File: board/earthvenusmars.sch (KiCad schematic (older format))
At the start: 24 parts, among them J4 Conn_01x04, SW1 SW_SPST, SW2 SW_SPST, SW3 SW_SPST, U1 ATSAMD21G18A-AU, U2 MIC5504-3.3YM5, Y1 32768Hz

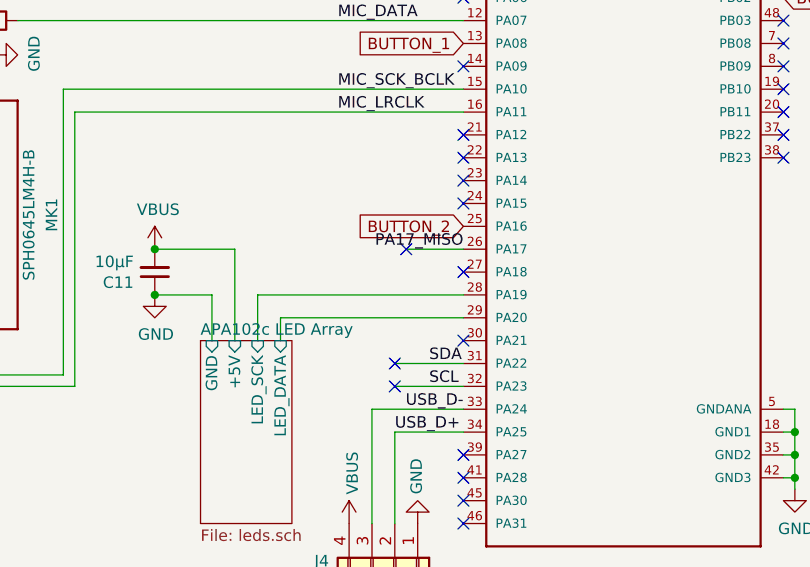
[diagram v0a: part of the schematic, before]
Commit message: move button 2 to pin 30 to avoid a via
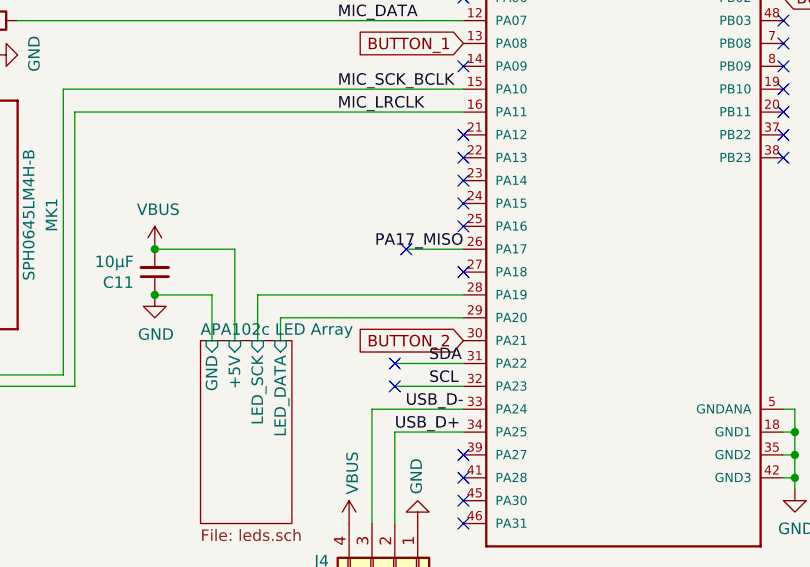
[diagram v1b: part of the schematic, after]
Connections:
- net BUTTON_2: now also U1.30 (PA21); no longer U1.25 (PA16)
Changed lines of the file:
@@
 NoConn ~ 5350 2950
 NoConn ~ 3950 3450
-NoConn ~ 3950 3750
+NoConn ~ 3950 3250
 NoConn ~ 3950 4250
 NoConn ~ 3950 4350
@@
 Text GLabel 3950 2450 0    50   Input ~ 0
 BUTTON_1
-Text GLabel 3950 3250 0    50   Input ~ 0
+Text GLabel 3950 3750 0    50   Input ~ 0
 BUTTON_2
 Text GLabel 5350 2250 2    50   Input ~ 0

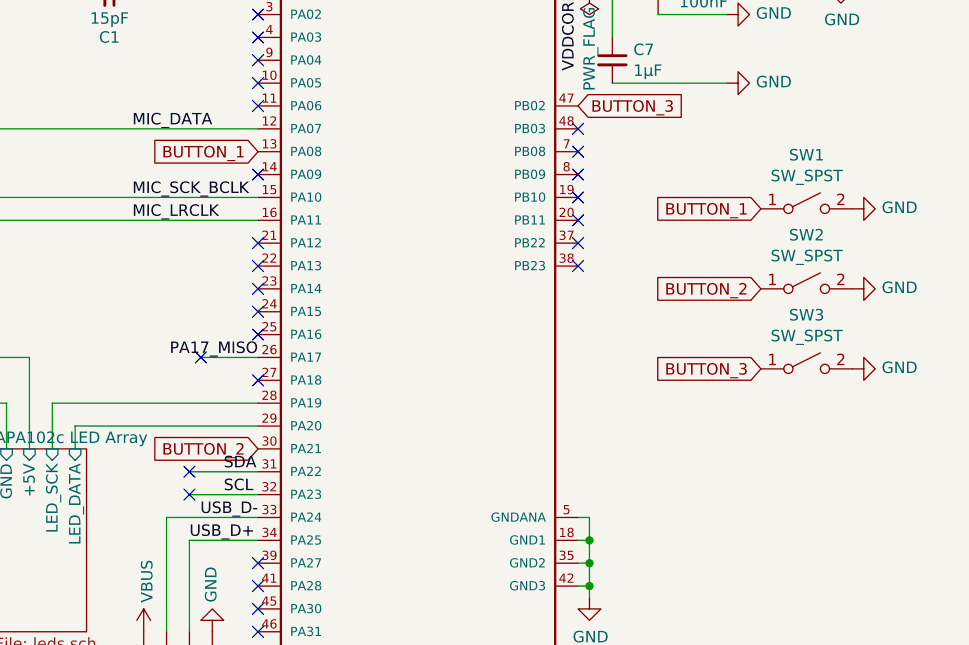
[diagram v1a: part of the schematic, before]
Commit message: proof of concept for entering low-power state when the brightness dial is all the way down, using the adc, then waking the system back up when the brightness dial is turned up again
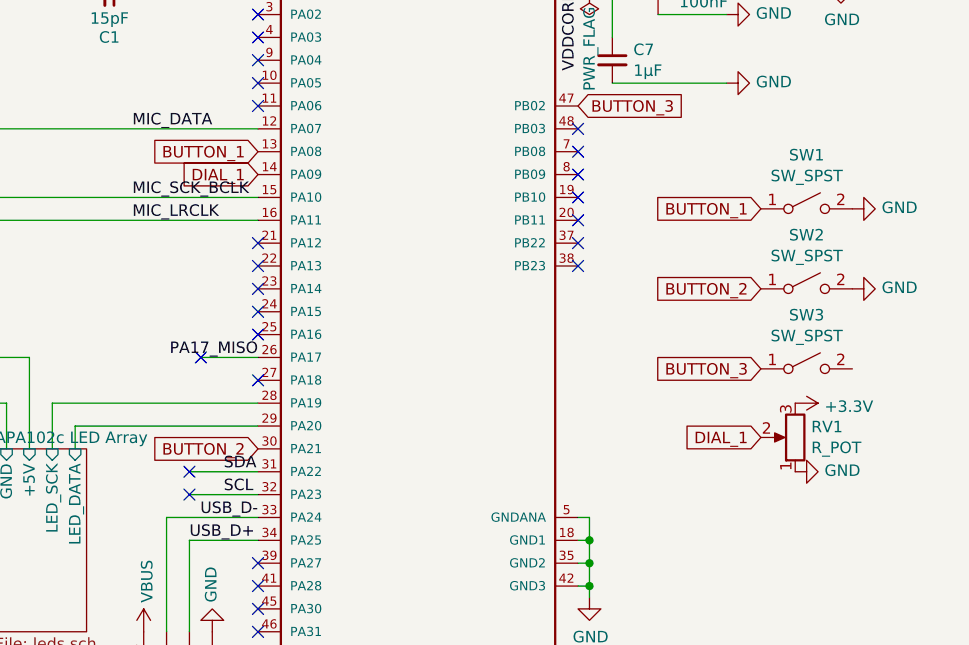
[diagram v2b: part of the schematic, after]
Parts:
- added RV1: R_POT, Pot_dial_3352T-1-103LF:Pot_dial_3352T-1-103LF, symbol Device:R_POT
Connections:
- net +3V3: now also RV1.3
- net GND: now also RV1.1; no longer SW3.2 (B)
- net DIAL_1: now reaches U1.14 (PA09)
- net DIAL_1: now also RV1.2
- no-connect marks 26 -> 25
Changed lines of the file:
@@
 NoConn ~ 3950 2950
 NoConn ~ 3950 2850
-NoConn ~ 3950 2550
 NoConn ~ 3950 2250
 NoConn ~ 3950 2150
@@
 $EndComp
 $Comp
-L power:GND #PWR?
+L power:GND #PWR0133
 U 1 1 5F9110A0
 P 6550 2700
-F 0 "#PWR?" H 6550 2450 50  0001 C CNN
+F 0 "#PWR0133" H 6550 2450 50  0001 C CNN
 F 1 "GND" V 6555 2572 50  0000 R CNN
 F 2 "" H 6550 2700 50  0001 C CNN
@@
 $EndComp
 $Comp
-L power:GND #PWR?
+L power:GND #PWR0134
 U 1 1 5F911146
 P 6550 3050
-F 0 "#PWR?" H 6550 2800 50  0001 C CNN
+F 0 "#PWR0134" H 6550 2800 50  0001 C CNN
 F 1 "GND" V 6555 2922 50  0000 R CNN
 F 2 "" H 6550 3050 50  0001 C CNN
@@
 $EndComp
 $Comp
-L power:GND #PWR?
+L power:GND #PWR0135
 U 1 1 5F9113D1
-P 6550 3400
-F 0 "#PWR?" H 6550 3150 50  0001 C CNN
-F 1 "GND" V 6555 3272 50  0000 R CNN
-F 2 "" H 6550 3400 50  0001 C CNN
-F 3 "" H 6550 3400 50  0001 C CNN
-	1    6550 3400
+P 6300 3850
+F 0 "#PWR0135" H 6300 3600 50  0001 C CNN
+F 1 "GND" V 6305 3722 50  0000 R CNN
+F 2 "" H 6300 3850 50  0001 C CNN
+F 3 "" H 6300 3850 50  0001 C CNN
+	1    6300 3850
 	0    -1   -1   0
 $EndComp
@@
 Text GLabel 6150 2700 0    50   Input ~ 0
 BUTTON_1
+$Comp
+L Device:R_POT RV1
+U 1 1 5FA0CDD3
+P 6300 3700
+F 0 "RV1" H 6230 3654 50  0000 R CNN
+F 1 "R_POT" H 6230 3745 50  0000 R CNN
+F 2 "Pot_dial_3352T-1-103LF:Pot_dial_3352T-1-103LF" H 6300 3700 50  0001 C CNN
+F 3 "~" H 6300 3700 50  0001 C CNN
+	1    6300 3700
+	-1   0    0    1
+$EndComp
+Text GLabel 3950 2550 0    50   Input ~ 0
+DIAL_1
+Text GLabel 6150 3700 0    50   Input ~ 0
+DIAL_1
+$Comp
+L power:+3.3V #PWR0136
+U 1 1 5FBE3505
+P 6300 3550
+F 0 "#PWR0136" H 6300 3400 50  0001 C CNN
+F 1 "+3.3V" V 6315 3678 50  0000 L CNN
+F 2 "" H 6300 3550 50  0001 C CNN
+F 3 "" H 6300 3550 50  0001 C CNN
+	1    6300 3550
+	0    1    1    0
+$EndComp
 $EndSCHEMATC

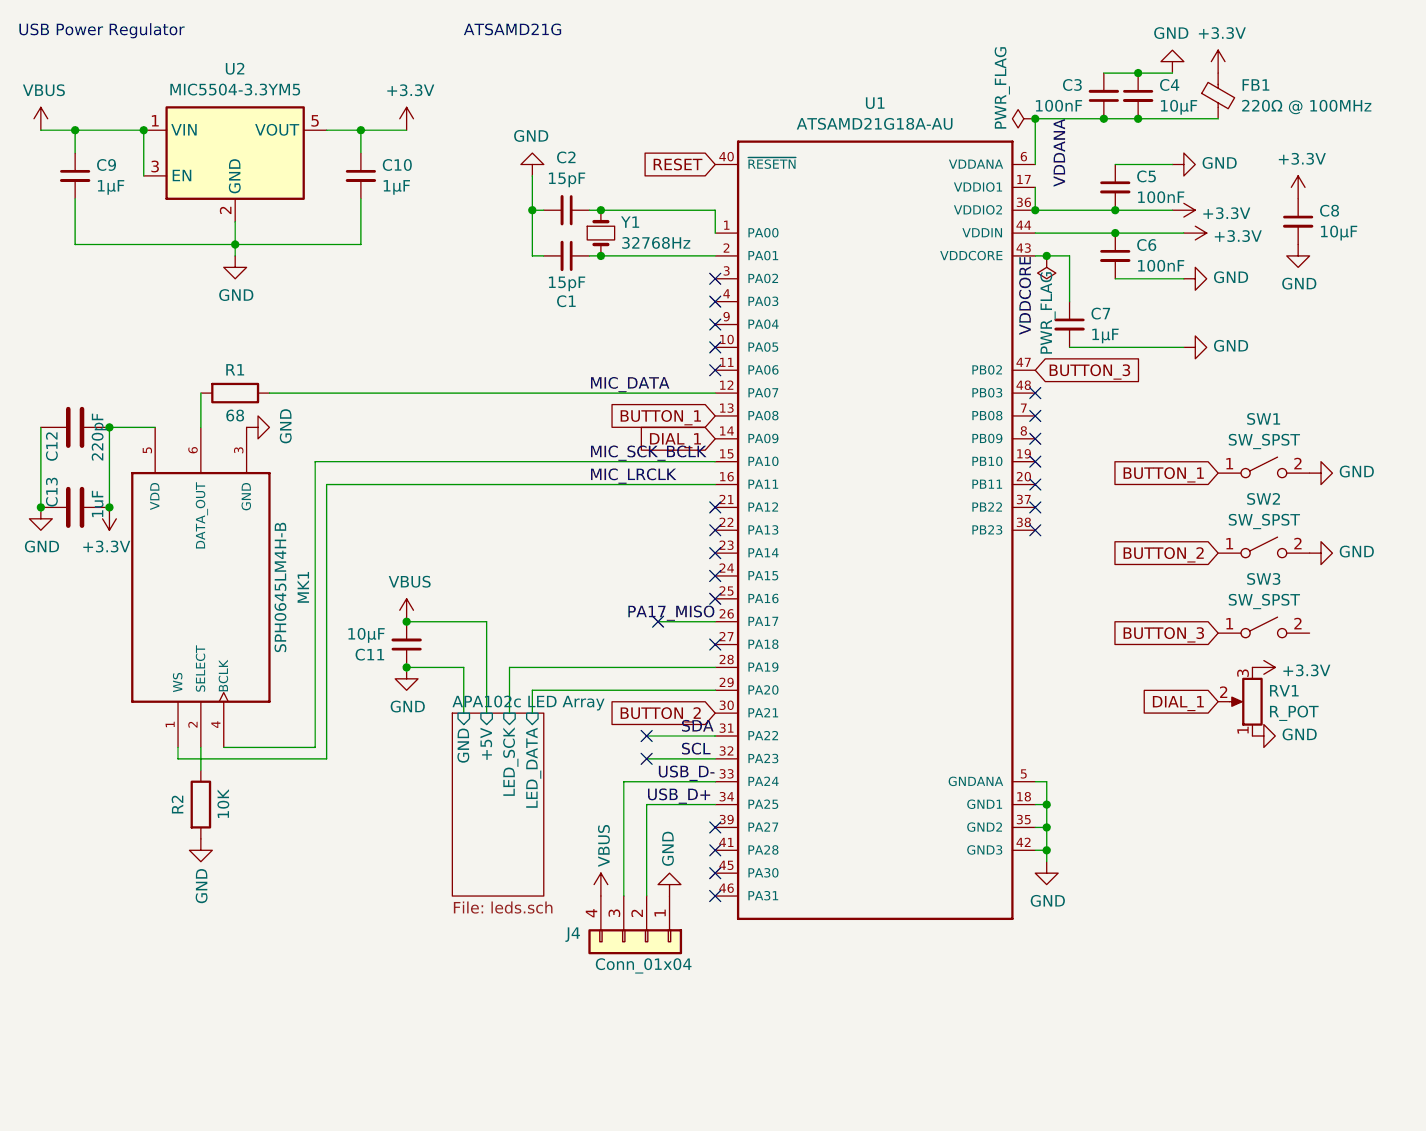
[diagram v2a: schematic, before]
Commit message: add pads on back for bootloader programming/reset and for driving the leds externally
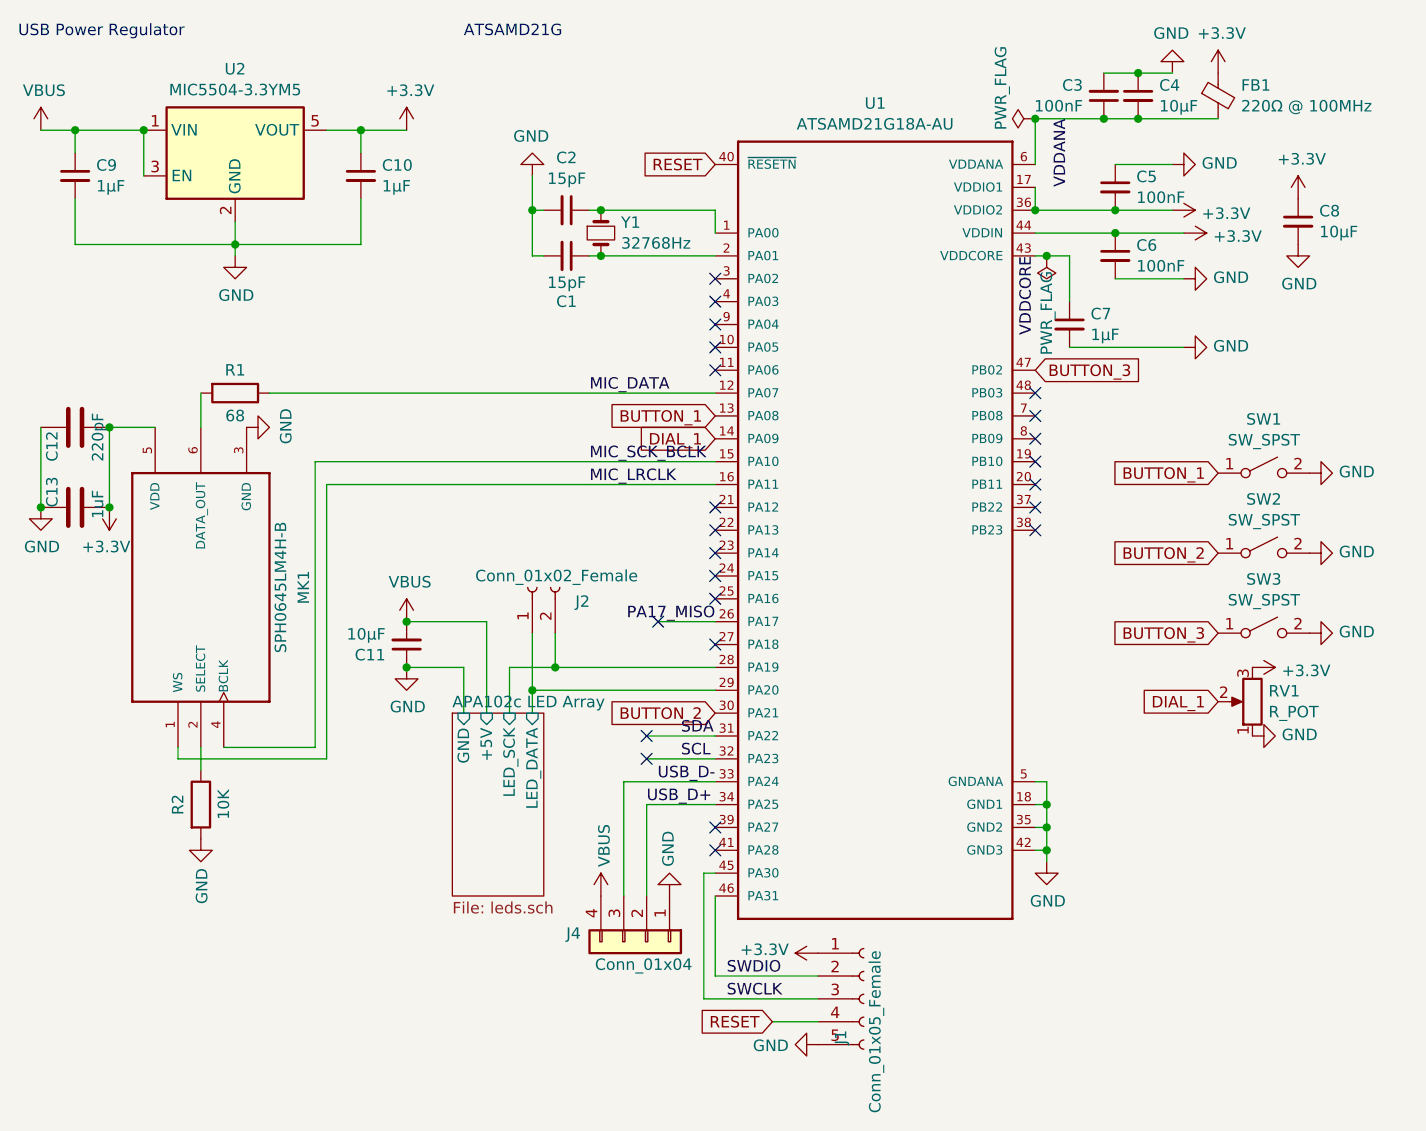
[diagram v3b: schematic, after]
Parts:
- added J1: Conn_01x05_Female, Pad_SMD:Pad_SMD_1.27mm_01x05, symbol Connector:Conn_01x05_Female
- added J2: Conn_01x02_Female, Pad_SMD:Pad_SMD_1.27mm_01x02, symbol Connector:Conn_01x02_Female
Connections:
- net +3V3: now also J1.1 (Pin_1)
- net APA102c LED Array/LED_DATA: now also J2.1 (Pin_1)
- net APA102c LED Array/LED_SCK: now also J2.2 (Pin_2)
- net GND: now also SW3.2 (B), J1.5 (Pin_5)
- net RESET: now also J1.4 (Pin_4)
- net SWCLK: now reaches U1.45 (PA30)
- net SWCLK: now also J1.3 (Pin_3)
- net SWDIO: now reaches U1.46 (PA31)
- net SWDIO: now also J1.2 (Pin_2)
- no-connect marks 25 -> 23
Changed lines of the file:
@@
 NoConn ~ 3950 4250
 NoConn ~ 3950 4350
-NoConn ~ 3950 4450
-NoConn ~ 3950 4550
 Wire Wire Line
 	3950 3350 3700 3350
@@
 F 3 "~" H 6350 2700 50  0001 C CNN
 	1    6350 2700
-	1    0    0    -1
-$EndComp
-$Comp
-L ATSAMD21G18A-AU:ATSAMD21G18A-AU U1
-U 1 1 5EB21719
-P 4650 2950
-F 0 "U1" H 4650 4817 50  0000 C CNN
-F 1 "ATSAMD21G18A-AU" H 4650 4726 50  0000 C CNN
-F 2 "ATSAMD21G18A-AU:ATSAMD21G18A-AU" H 4650 2950 50  0001 L BNN
-F 3 "ATMEL" H 4650 2950 50  0001 L BNN
-	1    4650 2950
 	1    0    0    -1
 $EndComp
@@
 	3050 3750 3050 3550
 Wire Wire Line
-	3050 3550 3950 3550
+	3050 3550 3250 3550
 Wire Wire Line
 	2850 3550 2850 3750
@@
 	0    1    1    0
 $EndComp
+$Comp
+L Connector:Conn_01x05_Female J1
+U 1 1 5FBFDA7E
+P 4600 5000
+F 0 "J1" V 4500 4800 50  0000 L CNN
+F 1 "Conn_01x05_Female" V 4650 4500 50  0000 L CNN
+F 2 "Pad_SMD:Pad_SMD_1.27mm_01x05" H 4600 5000 50  0001 C CNN
+F 3 "~" H 4600 5000 50  0001 C CNN
+	1    4600 5000
+	1    0    0    -1
+$EndComp
+$Comp
+L power:GND #PWR0137
+U 1 1 5FBFE728
+P 6550 3400
+F 0 "#PWR0137" H 6550 3150 50  0001 C CNN
+F 1 "GND" V 6555 3272 50  0000 R CNN
+F 2 "" H 6550 3400 50  0001 C CNN
+F 3 "" H 6550 3400 50  0001 C CNN
+	1    6550 3400
+	0    -1   -1   0
+$EndComp
+$Comp
+L ATSAMD21G18A-AU:ATSAMD21G18A-AU U1
+U 1 1 5EB21719
+P 4650 2950
+F 0 "U1" H 4650 4817 50  0000 C CNN
+F 1 "ATSAMD21G18A-AU" H 4650 4726 50  0000 C CNN
+F 2 "ATSAMD21G18A-AU:ATSAMD21G18A-AU" H 4650 2950 50  0001 L BNN
+F 3 "ATMEL" H 4650 2950 50  0001 L BNN
+	1    4650 2950
+	1    0    0    -1
+$EndComp
+Wire Wire Line
+	3950 4450 3900 4450
+Wire Wire Line
+	4200 5100 4400 5100
+Text GLabel 4200 5100 0    50   Input ~ 0
+RESET
+Wire Wire Line
+	3900 5000 4400 5000
+Wire Wire Line
+	3900 4450 3900 5000
+Wire Wire Line
+	3950 4550 3950 4900
+Wire Wire Line
+	3950 4900 4400 4900
+Text Label 4000 4900 0    50   ~ 0
+SWDIO
+Text Label 4000 5000 0    50   ~ 0
+SWCLK
+$Comp
+L Connector:Conn_01x02_Female J2
+U 1 1 5FC334AA
+P 3150 3200
+F 0 "J2" V 3088 3012 50  0000 R CNN
+F 1 "Conn_01x02_Female" V 3200 3450 50  0000 R CNN
+F 2 "Pad_SMD:Pad_SMD_1.27mm_01x02" H 3150 3200 50  0001 C CNN
+F 3 "~" H 3150 3200 50  0001 C CNN
+	1    3150 3200
+	0    -1   -1   0
+$EndComp
+Wire Wire Line
+	3150 3650 3150 3400
+Connection ~ 3150 3650
+Wire Wire Line
+	3250 3550 3250 3400
+Connection ~ 3250 3550
+Wire Wire Line
+	3250 3550 3950 3550
+$Comp
+L power:GND #PWR0138
+U 1 1 5FC4F9CF
+P 4400 5200
+F 0 "#PWR0138" H 4400 4950 50  0001 C CNN
+F 1 "GND" V 4405 5072 50  0000 R CNN
+F 2 "" H 4400 5200 50  0001 C CNN
+F 3 "" H 4400 5200 50  0001 C CNN
+	1    4400 5200
+	0    1    1    0
+$EndComp
+$Comp
+L power:+3.3V #PWR0139
+U 1 1 5FC5014A
+P 4400 4800
+F 0 "#PWR0139" H 4400 4650 50  0001 C CNN
+F 1 "+3.3V" V 4415 4928 50  0000 L CNN
+F 2 "" H 4400 4800 50  0001 C CNN
+F 3 "" H 4400 4800 50  0001 C CNN
+	1    4400 4800
+	0    -1   -1   0
+$EndComp
 $EndSCHEMATC

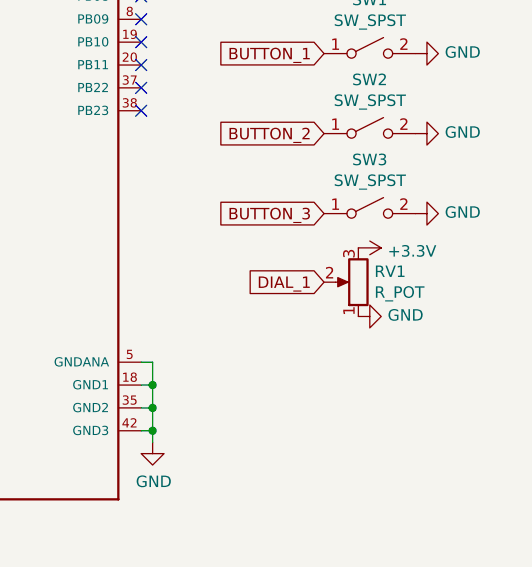
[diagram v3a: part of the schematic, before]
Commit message: add footprint for 3-hole safety pin attachment point; place 3 attachments on board; scoot things around for neatness/GND flow
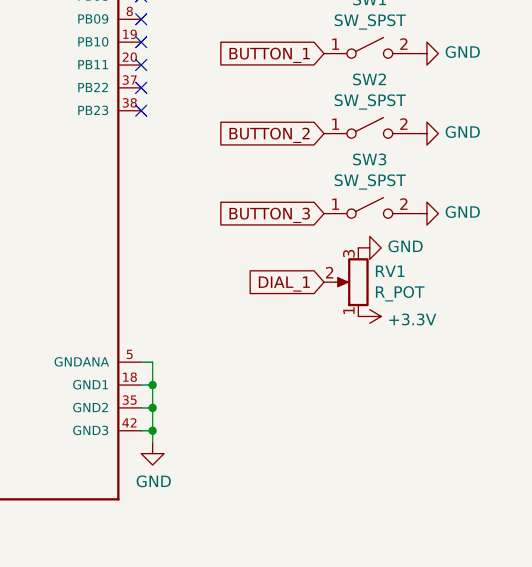
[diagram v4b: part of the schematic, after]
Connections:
- net +3V3: now also RV1.1; no longer RV1.3
- net GND: now also RV1.3; no longer RV1.1
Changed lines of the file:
@@
 L power:GND #PWR0135
 U 1 1 5F9113D1
-P 6300 3850
-F 0 "#PWR0135" H 6300 3600 50  0001 C CNN
-F 1 "GND" V 6305 3722 50  0000 R CNN
-F 2 "" H 6300 3850 50  0001 C CNN
-F 3 "" H 6300 3850 50  0001 C CNN
-	1    6300 3850
+P 6300 3550
+F 0 "#PWR0135" H 6300 3300 50  0001 C CNN
+F 1 "GND" V 6305 3422 50  0000 R CNN
+F 2 "" H 6300 3550 50  0001 C CNN
+F 3 "" H 6300 3550 50  0001 C CNN
+	1    6300 3550
 	0    -1   -1   0
 $EndComp
@@
 L power:+3.3V #PWR0136
 U 1 1 5FBE3505
-P 6300 3550
-F 0 "#PWR0136" H 6300 3400 50  0001 C CNN
-F 1 "+3.3V" V 6315 3678 50  0000 L CNN
-F 2 "" H 6300 3550 50  0001 C CNN
-F 3 "" H 6300 3550 50  0001 C CNN
-	1    6300 3550
+P 6300 3850
+F 0 "#PWR0136" H 6300 3700 50  0001 C CNN
+F 1 "+3.3V" V 6315 3978 50  0000 L CNN
+F 2 "" H 6300 3850 50  0001 C CNN
+F 3 "" H 6300 3850 50  0001 C CNN
+	1    6300 3850
 	0    1    1    0
 $EndComp

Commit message: add part number to a "Designation" field that will be output by the bom_csv_grouped_by_value script that looks like a better alternative than what I sent to the fab this time; remove (opal) from parts in .sch
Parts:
- FB1: Designation (none) -> BLM03HB191SN1D
- SW1, SW2, SW3: footprint Button_Switch_SMD:KMR731NG LFS (opal) -> Button_Switch_SMD:KMR731NG_LFS; Designation (none) -> KMR731NGLFS
- Y1: Designation (none) -> ECS-.327-12.5-34B-TR
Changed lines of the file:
@@
 F 2 "Crystal:Crystal_SMD_3215-2Pin_3.2x1.5mm" H 3450 1650 50  0001 C CNN
 F 3 "~" H 3450 1650 50  0001 C CNN
+F 4 "ECS-.327-12.5-34B-TR" H 3450 1650 50  0001 C CNN "Designation"
 	1    3450 1650
 	0    1    1    0
@@
 F 2 "Inductor_SMD:L_0201_0603Metric" V 6080 1050 50  0001 C CNN
 F 3 "~" H 6150 1050 50  0001 C CNN
+F 4 "BLM03HB191SN1D" H 6150 1050 50  0001 C CNN "Designation"
 	1    6150 1050
 	1    0    0    -1
@@
 F 0 "SW1" H 6350 2935 50  0000 C CNN
 F 1 "SW_SPST" H 6350 2844 50  0000 C CNN
-F 2 "Button_Switch_SMD:KMR731NG LFS (opal)" H 6350 2700 50  0001 C CNN
+F 2 "Button_Switch_SMD:KMR731NG_LFS" H 6350 2700 50  0001 C CNN
 F 3 "~" H 6350 2700 50  0001 C CNN
+F 4 "KMR731NGLFS" H 6350 2700 50  0001 C CNN "Designation"
 	1    6350 2700
 	1    0    0    -1
@@
 F 0 "SW2" H 6350 3285 50  0000 C CNN
 F 1 "SW_SPST" H 6350 3194 50  0000 C CNN
-F 2 "Button_Switch_SMD:KMR731NG LFS (opal)" H 6350 3050 50  0001 C CNN
+F 2 "Button_Switch_SMD:KMR731NG_LFS" H 6350 3050 50  0001 C CNN
 F 3 "~" H 6350 3050 50  0001 C CNN
+F 4 "KMR731NGLFS" H 6350 3050 50  0001 C CNN "Designation"
 	1    6350 3050
 	1    0    0    -1
@@
 F 0 "SW3" H 6350 3635 50  0000 C CNN
 F 1 "SW_SPST" H 6350 3544 50  0000 C CNN
-F 2 "Button_Switch_SMD:KMR731NG LFS (opal)" H 6350 3400 50  0001 C CNN
+F 2 "Button_Switch_SMD:KMR731NG_LFS" H 6350 3400 50  0001 C CNN
 F 3 "~" H 6350 3400 50  0001 C CNN
+F 4 "KMR731NGLFS" H 6350 3400 50  0001 C CNN "Designation"
 	1    6350 3400
 	1    0    0    -1
